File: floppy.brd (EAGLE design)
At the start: 88.6 x 93.7 mm, 18 parts, among them IC1 ATTINY13-20SU, Q1 S9018

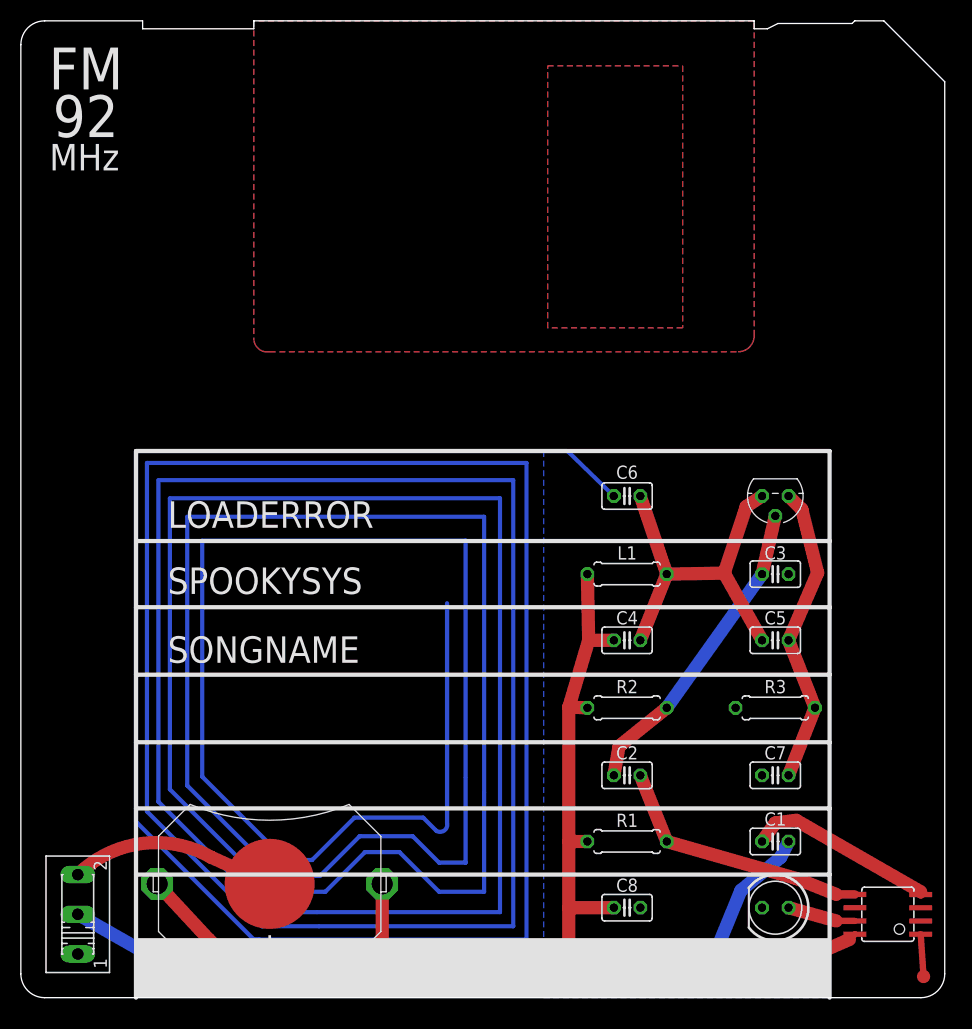
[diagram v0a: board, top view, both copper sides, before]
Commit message: New circuit that has been tested to work up front
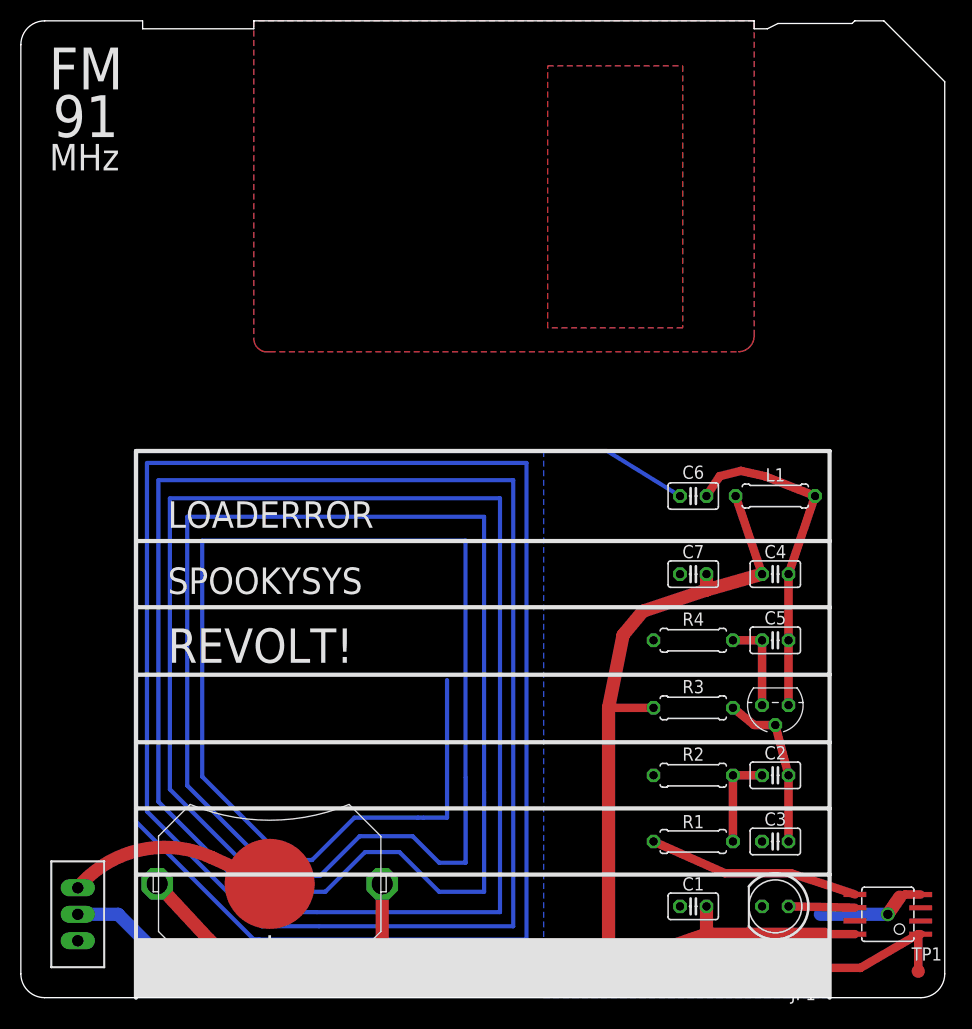
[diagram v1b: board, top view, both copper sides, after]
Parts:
- removed C8: 0.1uF, rcl:C025-025X050
- removed DW: TPB1,27, testpad:B1,27
- added JP1: (no value), pinhead:1X03
- added R4: 470, rcl:0207/7
- added TP1: TPB1,27, testpad:B1,27
- C2: value 0.1uF -> 100nF
- C3: value 680pF -> 1nF
- C4: value 30pF -> 47pF
- C5: value 10pF -> 5.6pF
- C6: value 30pF -> 27pF
- C7: value 30pF -> 22nF
- L1: value 100nH -> ~250nH??
- Q1: value S9018 -> BC547
- R1: value 2.2K -> 22K
- R2: value 22K -> 470
- R3: value 2.2K -> 47K
- S1: value (none) -> TL36PO; device switch:255SB -> switch:TL3XPO
- moved C3 25.7 mm to (72.4, 15.0), turned to 180 degrees
- moved C7 20.8 mm to (64.5, 40.6)
- moved Q1 20.1 mm to (72.4, 28.1)
- moved L1 16.1 mm to (72.4, 48.1)
- moved C4 15.6 mm to (72.4, 40.6)
- moved C2 14.2 mm to (72.4, 21.3), turned to 0 degrees
- moved C1 10.0 mm to (64.5, 8.76)
- moved R2 9.07 mm to (64.5, 21.3)
- moved R3 7.87 mm to (64.5, 27.8), turned to 180 degrees
- moved C6 6.35 mm to (64.5, 48.1)
- moved R1 6.35 mm to (64.5, 15.0)
- moved LED1 0.13 mm to (72.4, 8.76)
- turned C5 to 180 degrees
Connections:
- new net N$4: IC1.5, R1.2
- net AUDIO: now also R2.1; no longer IC1.5
- net DW: now also JP1.1, TP1.TP; no longer DW.TP
- net GND: now also JP1.2, R2.2, R4.1; no longer C8.2, R3.1
- net N$5: now also IC1.6; no longer IC1.7
- net N$6: now also Q1.3; no longer Q1.1
- net N$7: now also Q1.1, R4.2; no longer C7.1, Q1.3, R3.2
- net N$8: now also R3.1; no longer R2.1
- net VCC: now also C7.1, JP1.3, R3.2; no longer C8.1, R1.2, R2.2
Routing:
- net N$4: track 0.00 -> 20.3 mm
- net N$7: track 29.0 -> 9.02 mm
- net AUDIO: track 25.7 -> 9.14 mm
- net N$8: track 30.2 -> 16.0 mm
- net DW: track 4.07 -> 15.8 mm
- net GND: track 65.2 -> 58.3 mm, vias 0 -> 1
- net N$6: track 36.2 -> 32.4 mm
- net VCC: track 141.7 -> 145.1 mm, vias 1 -> 0
- net ANT: track 814.9 -> 812.1 mm
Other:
- board text added: "#fm-revolt warning illegal radio transmitter"
- board text added: "91"
- board text added: "REVOLT!"
- board text removed: "92"
- board text removed: "SONGNAME"
- board text removed: "Warning: Illegal radio transmitter"
